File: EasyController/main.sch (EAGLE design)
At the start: 50 parts, among them IC2 L6387EDIP8, IC3 L6387EDIP8, IC4 L6387EDIP8, J3 FUSE, Q1 MOSFET-NCHANNELTO-220-FLAT, Q2 MOSFET-NCHANNELTO-220-FLAT, Q3 MOSFET-NCHANNELTO-220-FLAT, Q4 MOSFET-NCHANNELTO-220-FLAT, Q5 MOSFET-NCHANNELTO-220-FLAT, Q6 MOSFET-NCHANNELTO-220-FLAT

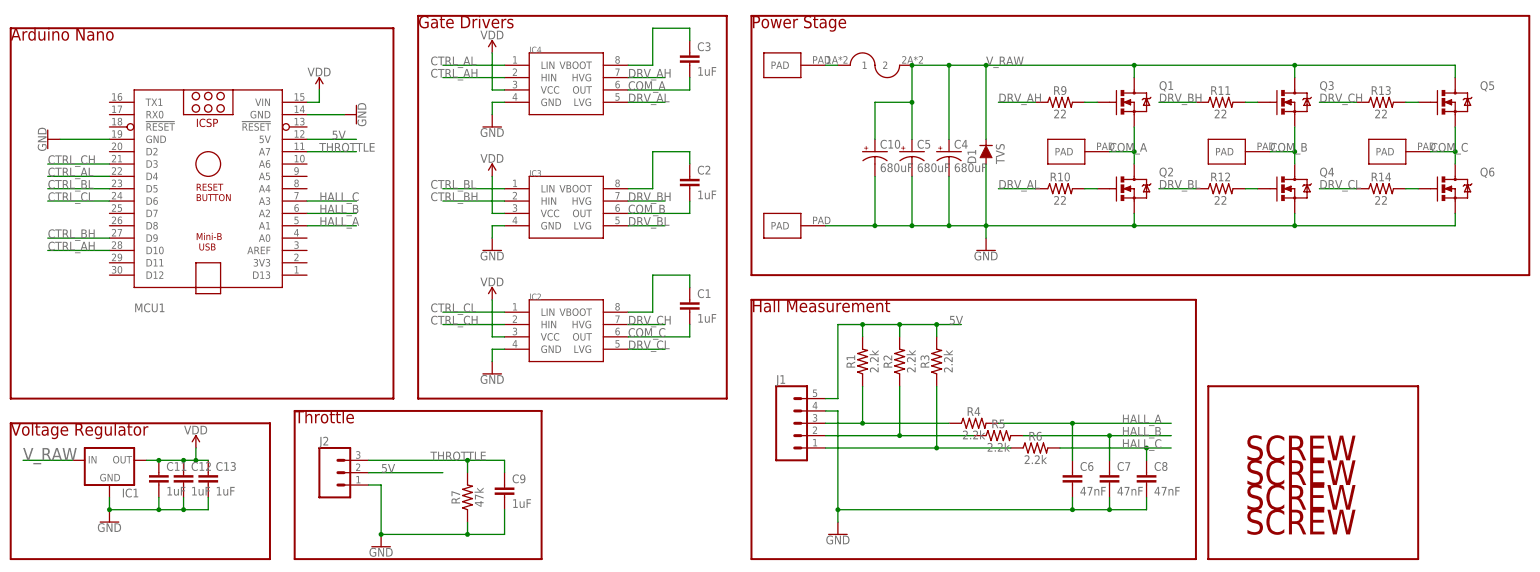
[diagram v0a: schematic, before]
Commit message: EasyController and EasyTelemetry almost ready to submit
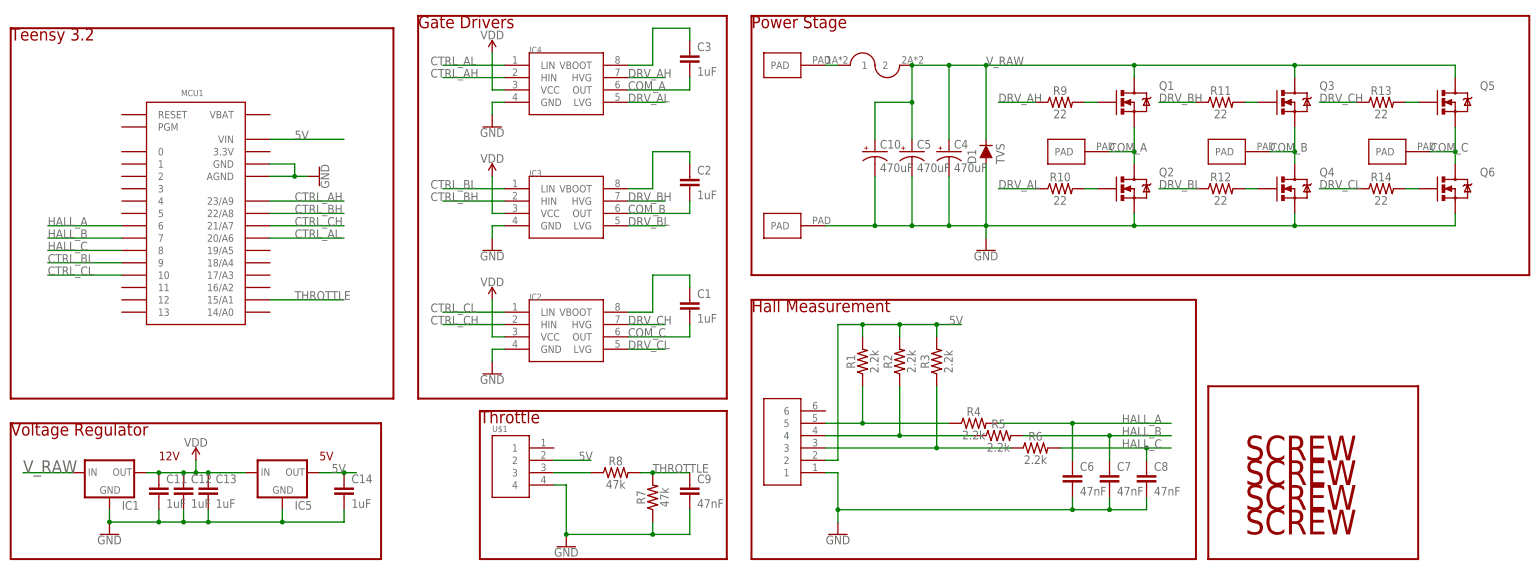
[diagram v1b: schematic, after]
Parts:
- removed J1: (no value), SparkFun-Connectors:CONN_05
- removed J2: (no value), SparkFun-Connectors:CONN_03
- added C14: 1uF, SparkFun-Capacitors:0.1UF-KIT-EZ-50V-20%
- added IC5: (no value), SparkFun-IC-Power:V_REG_78XXTO-92_UNTESTED
- added R8: 47k, SparkFun-Resistors:RESISTORAXIAL-0.3
- added U$1: HEADER4VALULOK, Custom_old:HEADER4VALULOK
- added U$2: HEADER6, Custom_old:HEADER6
- C10, C4, C5: value 680uF -> 470uF
- C9: value 1uF -> 47nF
- MCU1: value (none) -> TEENSY_3.0_BASIC; device ArduinoNanoV30:ARDUINO_NANO -> Teensy3.0:TEENSY_3.0_BASIC
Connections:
- new net N$7: R8.1, U$1.3
- net 5V: now also C14.1, IC5.OUT, MCU1.VIN, U$1.2, U$2.2; no longer J1.5, J2.2, MCU1.5V
- net CTRL_AH: now also MCU1.23/A9; no longer MCU1.D10
- net CTRL_AL: now also MCU1.20/A6; no longer MCU1.D4
- net CTRL_BH: now also MCU1.22/A8; no longer MCU1.D9
- net CTRL_BL: now also MCU1.9; no longer MCU1.D5
- net CTRL_CH: now also MCU1.21/A7; no longer MCU1.D3
- net CTRL_CL: now also MCU1.10; no longer MCU1.D6
- net GND: now also C14.2, IC5.GND, MCU1.AGND, MCU1.GND, U$1.4, U$2.1; no longer J1.4, J2.1, MCU1.GND@1, MCU1.GND@2
- net HALL_A: now also MCU1.6; no longer MCU1.A1
- net HALL_B: now also MCU1.7; no longer MCU1.A2
- net HALL_C: now also MCU1.8; no longer MCU1.A3
- net N$2: now also U$2.3; no longer J1.1
- net N$4: now also U$2.4; no longer J1.2
- net N$6: now also U$2.5; no longer J1.3
- net THROTTLE: now also MCU1.15/A1, R8.2; no longer J2.3, MCU1.A7
- net VDD: now also IC5.IN; no longer MCU1.VIN
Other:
- note added: "12V"
- note added: "5V"
- note added: "Teensy 3.2"
- note removed: "Arduino Nano"
- moved on the sheet: C11, C12, C13, C9, IC1, R7
